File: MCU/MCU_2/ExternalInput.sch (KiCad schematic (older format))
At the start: 49 parts, among them J14 Conn_01x02, J15 Conn_01x02, J16 Conn_01x02, J17 Conn_01x04, J18 Conn_01x02, J20 CAN, J21 Conn_01x04, Q13 DTA144E, Q14 DTA124E, Q15 DTC124E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

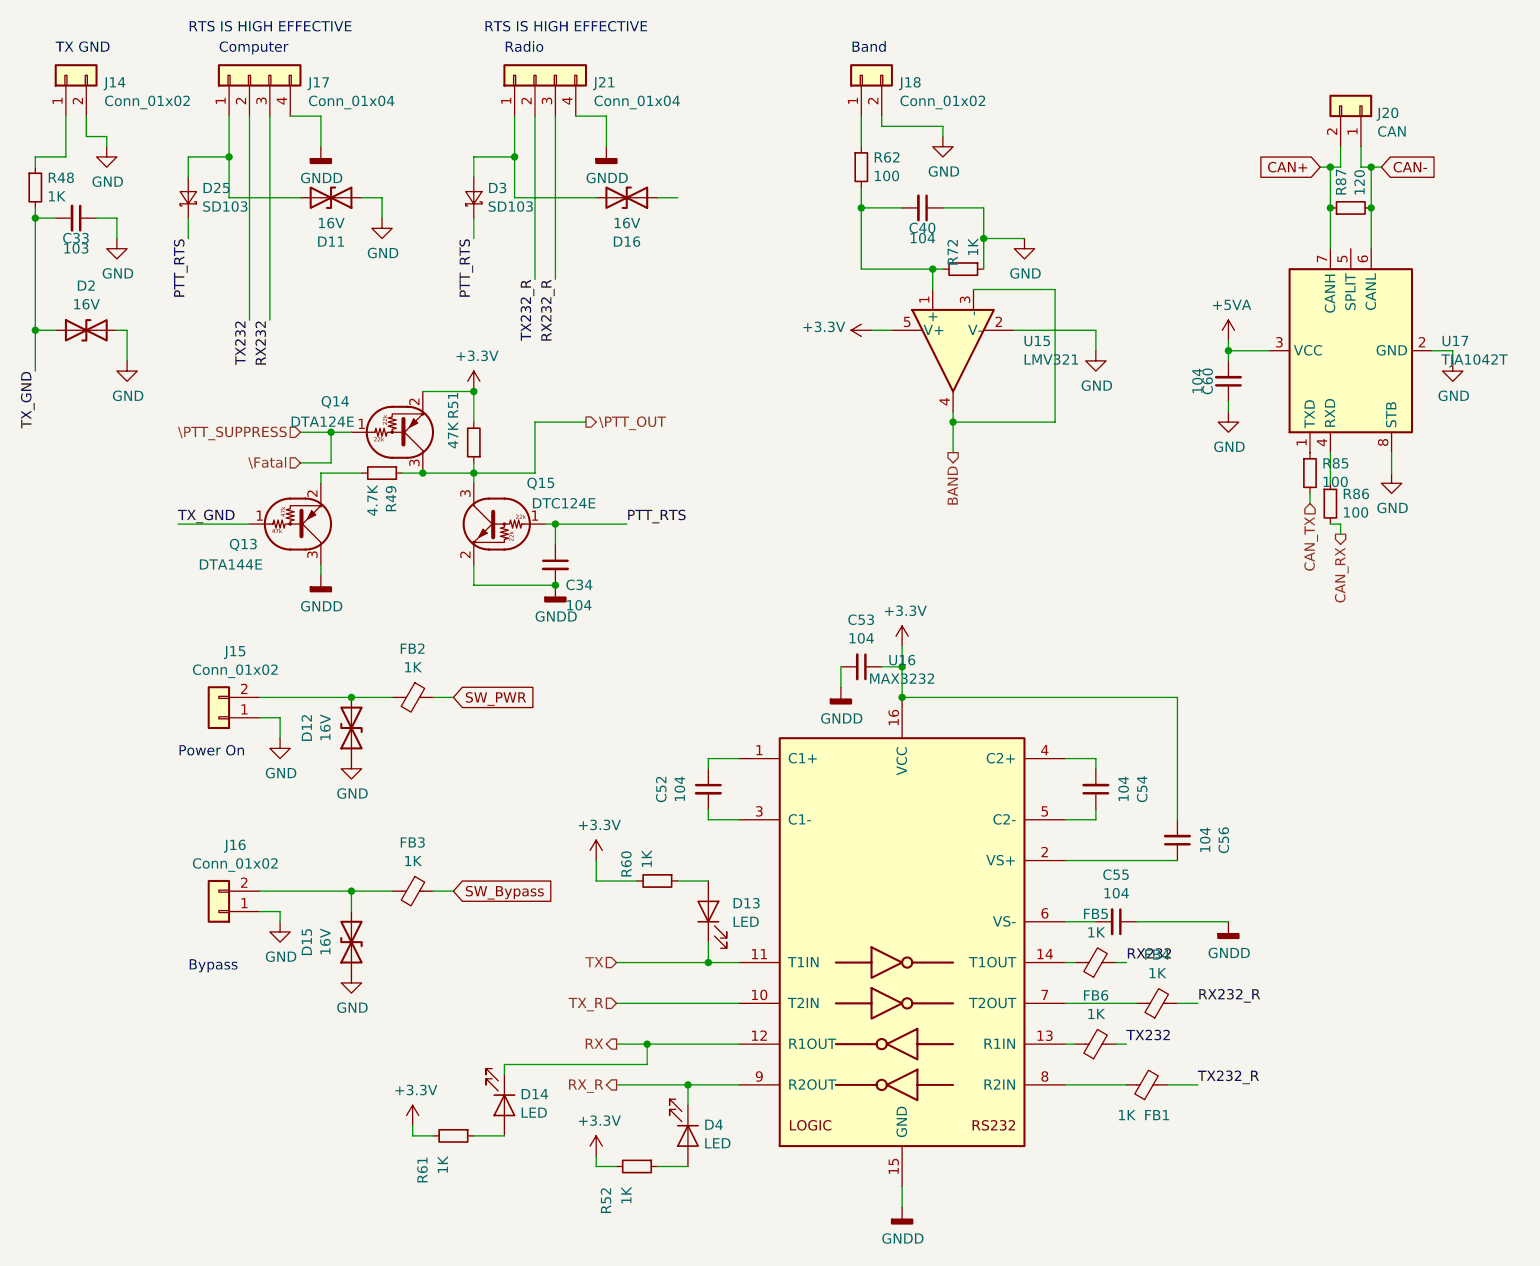
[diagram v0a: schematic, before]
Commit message: MCU PCB start layouting
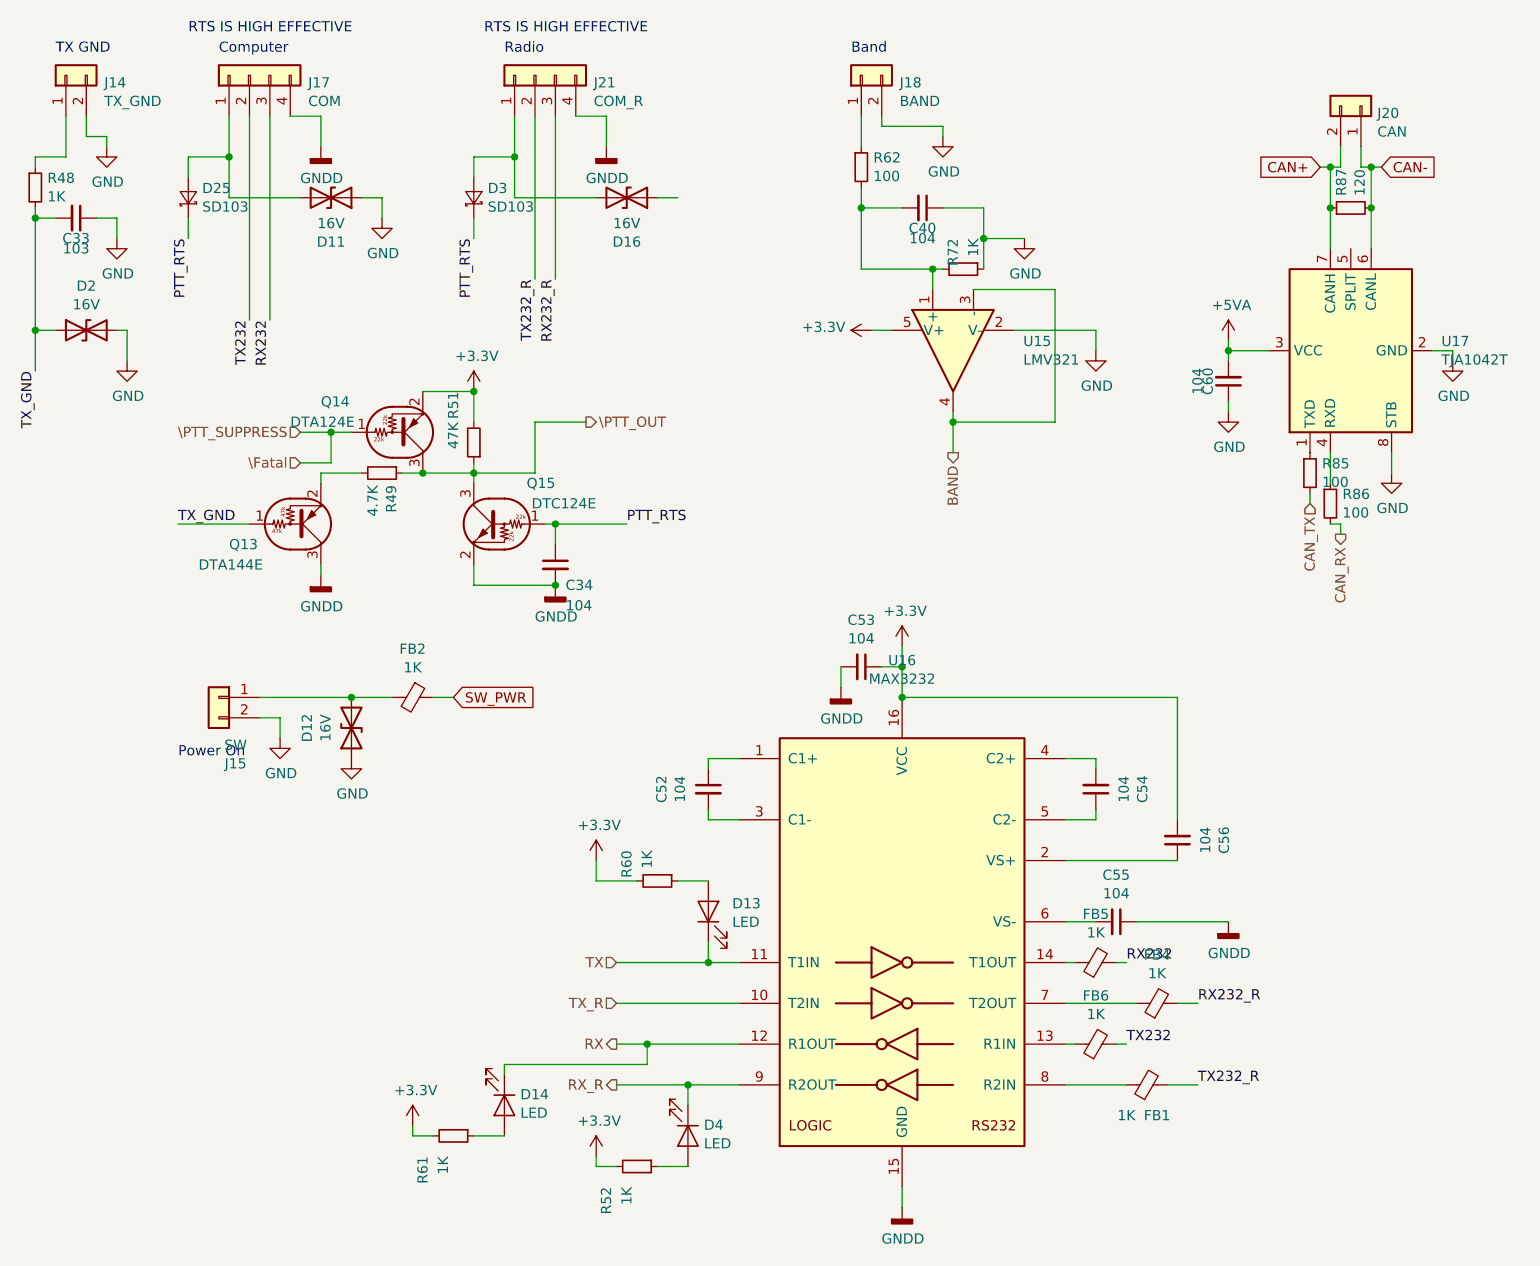
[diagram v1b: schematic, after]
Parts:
- removed D15: 16V, lc_lib:SMA(DO-214AC)_S4, symbol Device:D_TVS
- removed FB3: 1K, lc_lib:0805_R, symbol Device:Ferrite_Bead_Small
- removed J16: Conn_01x02, Connector_PinHeader_2.54mm:PinHeader_1x02_P2.54mm_Vertical, symbol Connector_Generic:Conn_01x02
- J14: value Conn_01x02 -> TX_GND
- J15: value Conn_01x02 -> SW
- J17: value Conn_01x04 -> COM
- J18: value Conn_01x02 -> BAND
- J21: value Conn_01x04 -> COM_R
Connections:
- net GND: now also J15.2 (Pin_2); no longer J15.1 (Pin_1)
- net at D12.2 (A2), FB2.2: now also J15.1 (Pin_1); no longer J15.2 (Pin_2)
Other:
- note removed: "Bypass"
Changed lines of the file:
@@
 AR Path="/5EA95119/5EA99E3C" Ref="J14"  Part="1"
 F 0 "J14" V 914 1812 50  0000 R CNN
-F 1 "Conn_01x02" V 823 1812 50  0000 R CNN
+F 1 "TX_GND" V 823 1812 50  0000 R CNN
 F 2 "Connector_PinHeader_2.54mm:PinHeader_1x02_P2.54mm_Vertical" H 950 2000 50  0001 C CNN
 F 3 "~" H 950 2000 50  0001 C CNN
@@
 AR Path="/5EA95119/5EA99E4D" Ref="J18"  Part="1"
 F 0 "J18" V 4814 1812 50  0000 R CNN
-F 1 "Conn_01x02" V 4723 1812 50  0000 R CNN
+F 1 "BAND" V 4723 1812 50  0000 R CNN
 F 2 "Connector_PinHeader_2.54mm:PinHeader_1x02_P2.54mm_Vertical" H 4850 2000 50  0001 C CNN
 F 3 "~" H 4850 2000 50  0001 C CNN
@@
 L Connector_Generic:Conn_01x02 J?
 U 1 1 5EA9F740
-P 1700 5150
+P 1700 5050
 AR Path="/5E814668/5EA9F740" Ref="J?"  Part="1"
 AR Path="/5EA95119/5EA9F740" Ref="J15"  Part="1"
-F 0 "J15" H 1618 4825 50  0000 C CNN
-F 1 "Conn_01x02" H 1618 4916 50  0000 C CNN
-F 2 "Connector_PinHeader_2.54mm:PinHeader_1x02_P2.54mm_Vertical" H 1700 5150 50  0001 C CNN
-F 3 "~" H 1700 5150 50  0001 C CNN
-	1    1700 5150
-	-1   0    0    1
+F 0 "J15" H 1618 4725 50  0000 C CNN
+F 1 "SW" H 1618 4816 50  0000 C CNN
+F 2 "Connector_PinHeader_2.54mm:PinHeader_1x02_P2.54mm_Vertical" H 1700 5050 50  0001 C CNN
+F 3 "~" H 1700 5050 50  0001 C CNN
+	1    1700 5050
+	-1   0    0    -1
 $EndComp
 $Comp
@@
 Text Notes 1500 5350 0    50   ~ 0
 Power On
-$Comp
-L Connector_Generic:Conn_01x02 J?
-U 1 1 5EAA244F
-P 1700 6100
-AR Path="/5E814668/5EAA244F" Ref="J?"  Part="1"
-AR Path="/5EA95119/5EAA244F" Ref="J16"  Part="1"
-F 0 "J16" H 1618 5775 50  0000 C CNN
-F 1 "Conn_01x02" H 1618 5866 50  0000 C CNN
-F 2 "Connector_PinHeader_2.54mm:PinHeader_1x02_P2.54mm_Vertical" H 1700 6100 50  0001 C CNN
-F 3 "~" H 1700 6100 50  0001 C CNN
-	1    1700 6100
-	-1   0    0    1
-$EndComp
-Text GLabel 2850 6000 2    50   Input ~ 0
-SW_Bypass
-$Comp
-L power:GND #PWR?
-U 1 1 5EAA2C57
-P 2000 6150
-AR Path="/5E814668/5EAA2C57" Ref="#PWR?"  Part="1"
-AR Path="/5EA95119/5EAA2C57" Ref="#PWR097"  Part="1"
-F 0 "#PWR097" H 2000 5900 50  0001 C CNN
-F 1 "GND" H 2005 5977 50  0000 C CNN
-F 2 "" H 2000 6150 50  0001 C CNN
-F 3 "" H 2000 6150 50  0001 C CNN
-	1    2000 6150
-	1    0    0    -1
-$EndComp
-Wire Wire Line
-	2000 6150 2000 6100
-Wire Wire Line
-	2000 6100 1900 6100
-Text Notes 1550 6400 0    50   ~ 0
-Bypass
 Text HLabel 5300 3850 3    50   Output ~ 0
 BAND
@@
 P 1850 2000
 F 0 "J17" V 1814 1712 50  0000 R CNN
-F 1 "Conn_01x04" V 1723 1712 50  0000 R CNN
+F 1 "COM" V 1723 1712 50  0000 R CNN
 F 2 "Connector_JST:JST_PH_B4B-PH-SM4-TB_1x04-1MP_P2.00mm_Vertical" H 1850 2000 50  0001 C CNN
 F 3 "~" H 1850 2000 50  0001 C CNN
@@
 Wire Wire Line
 	800  2400 950  2400
-$Comp
-L Device:Ferrite_Bead_Small FB3
-U 1 1 5E4A8DD2
-P 2650 6000
-F 0 "FB3" V 2413 6000 50  0000 C CNN
-F 1 "1K" V 2504 6000 50  0000 C CNN
-F 2 "lc_lib:0805_R" V 2580 6000 50  0001 C CNN
-F 3 "~" H 2650 6000 50  0001 C CNN
-	1    2650 6000
-	0    1    1    0
-$EndComp
 Wire Wire Line
 	800  2650 800  2700
 Wire Wire Line
 	1550 2700 1550 2800
-Wire Wire Line
-	2750 6000 2850 6000
 $Comp
 L power:GNDD #PWR0146
@@
 P 3250 2000
 F 0 "J21" V 3214 1712 50  0000 R CNN
-F 1 "Conn_01x04" V 3123 1712 50  0000 R CNN
+F 1 "COM_R" V 3123 1712 50  0000 R CNN
 F 2 "Connector_JST:JST_PH_B4B-PH-SM4-TB_1x04-1MP_P2.00mm_Vertical" H 3250 2000 50  0001 C CNN
 F 3 "~" H 3250 2000 50  0001 C CNN
@@
 SW_PWR
 $Comp
-L Device:D_TVS D15
-U 1 1 6188138C
-P 2350 6250
-F 0 "D15" H 2350 6467 50  0000 C CNN
-F 1 "16V" H 2350 6376 50  0000 C CNN
-F 2 "lc_lib:SMA(DO-214AC)_S4" H 2350 6250 50  0001 C CNN
-F 3 "~" H 2350 6250 50  0001 C CNN
-	1    2350 6250
-	0    -1   -1   0
-$EndComp
-$Comp
 L Device:D_TVS D12
 U 1 1 61881392
@@
 	1    0    0    -1
 $EndComp
-Wire Wire Line
-	1900 6000 2350 6000
-Wire Wire Line
-	2350 6100 2350 6000
-Connection ~ 2350 6000
-Wire Wire Line
-	2350 6000 2550 6000
-$Comp
-L power:GND #PWR?
-U 1 1 618B9365
-P 2350 6400
-AR Path="/5E814668/618B9365" Ref="#PWR?"  Part="1"
-AR Path="/5EA95119/618B9365" Ref="#PWR0118"  Part="1"
-F 0 "#PWR0118" H 2350 6150 50  0001 C CNN
-F 1 "GND" H 2355 6227 50  0000 C CNN
-F 2 "" H 2350 6400 50  0001 C CNN
-F 3 "" H 2350 6400 50  0001 C CNN
-	1    2350 6400
-	1    0    0    -1
-$EndComp

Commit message: routing signals
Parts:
- removed C40: 104, lc_lib:0805_C, symbol Device:C_Small
- removed J18: BAND, Connector_PinHeader_2.54mm:PinHeader_1x02_P2.54mm_Vertical, symbol Connector_Generic:Conn_01x02
- removed R62: 100, lc_lib:0805_R, symbol Device:R_Small
- removed R72: 1K, lc_lib:0805_R, symbol Device:R_Small
- removed U15: LMV321, lc_lib:SOT-23-5, symbol Amplifier_Operational:LMV321
- J20: footprint Connector_JST:JST_PH_B2B-PH-SM4-TB_1x02-1MP_P2.00mm_Vertical -> Connector_PinHeader_2.54mm:PinHeader_1x02_P2.54mm_Vertical
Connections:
- net CAN+: now also J20.1 (Pin_1); no longer J20.2 (Pin_2)
- net CAN-: now also J20.2 (Pin_2); no longer J20.1 (Pin_1)
- net GND: now also D16.1 (A1)
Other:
- note removed: "Band"
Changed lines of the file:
@@
 $Descr A4 11693 8268
 encoding utf-8
-Sheet 4 5
+Sheet 3 5
 Title ""
 Date ""
@@
 Wire Wire Line
 	1050 2300 1050 2200
-$Comp
-L Connector_Generic:Conn_01x02 J?
-U 1 1 5EA99E4D
-P 4850 2000
-AR Path="/5E7D94C5/5EA99E4D" Ref="J?"  Part="1"
-AR Path="/5EA95119/5EA99E4D" Ref="J18"  Part="1"
-F 0 "J18" V 4814 1812 50  0000 R CNN
-F 1 "BAND" V 4723 1812 50  0000 R CNN
-F 2 "Connector_PinHeader_2.54mm:PinHeader_1x02_P2.54mm_Vertical" H 4850 2000 50  0001 C CNN
-F 3 "~" H 4850 2000 50  0001 C CNN
-	1    4850 2000
-	0    -1   -1   0
-$EndComp
-$Comp
-L power:GND #PWR?
-U 1 1 5EA99E55
-P 5250 2300
-AR Path="/5E7D94C5/5EA99E55" Ref="#PWR?"  Part="1"
-AR Path="/5EA95119/5EA99E55" Ref="#PWR099"  Part="1"
-F 0 "#PWR099" H 5250 2050 50  0001 C CNN
-F 1 "GND" H 5255 2127 50  0000 C CNN
-F 2 "" H 5250 2300 50  0001 C CNN
-F 3 "" H 5250 2300 50  0001 C CNN
-	1    5250 2300
-	1    0    0    -1
-$EndComp
-Wire Wire Line
-	4950 2250 4950 2200
 $Comp
 L Connector_Generic:Conn_01x02 J?
@@
 Text Notes 1500 5350 0    50   ~ 0
 Power On
-Text HLabel 5300 3850 3    50   Output ~ 0
-BAND
 Wire Wire Line
 	950  2200 950  2400
@@
 $EndComp
 $Comp
-L Device:R_Small R62
-U 1 1 5E2E974A
-P 4850 2450
-F 0 "R62" H 4909 2496 50  0000 L CNN
-F 1 "100" H 4909 2405 50  0000 L CNN
-F 2 "lc_lib:0805_R" H 4850 2450 50  0001 C CNN
-F 3 "~" H 4850 2450 50  0001 C CNN
-	1    4850 2450
-	1    0    0    -1
-$EndComp
-Wire Wire Line
-	4850 2550 4850 2650
-$Comp
-L Device:C_Small C40
-U 1 1 5E2EA49A
-P 5150 2650
-F 0 "C40" V 5250 2650 50  0000 C CNN
-F 1 "104" V 5300 2650 50  0000 C CNN
-F 2 "lc_lib:0805_C" H 5150 2650 50  0001 C CNN
-F 3 "~" H 5150 2650 50  0001 C CNN
-	1    5150 2650
-	0    1    1    0
-$EndComp
-Wire Wire Line
-	5050 2650 4850 2650
-$Comp
-L power:GND #PWR?
-U 1 1 5E2EAA47
-P 5650 2800
-AR Path="/5E7D94C5/5E2EAA47" Ref="#PWR?"  Part="1"
-AR Path="/5EA95119/5E2EAA47" Ref="#PWR0100"  Part="1"
-F 0 "#PWR0100" H 5650 2550 50  0001 C CNN
-F 1 "GND" H 5655 2627 50  0000 C CNN
-F 2 "" H 5650 2800 50  0001 C CNN
-F 3 "" H 5650 2800 50  0001 C CNN
-	1    5650 2800
-	1    0    0    -1
-$EndComp
-Text Notes 4800 1900 0    50   ~ 0
-Band
-$Comp
 L Interface_UART:MAX3232 U16
 U 1 1 5E403A54
@@
 Text HLabel 3650 6750 0    50   Output ~ 0
 RX
-$Comp
-L Device:R_Small R61
-U 1 1 5F387D6B
-P 2850 7200
-F 0 "R61" H 2950 7050 50  0000 L CNN
-F 1 "1K" H 2950 7150 50  0000 L CNN
-F 2 "lc_lib:0805_R" H 2850 7200 50  0001 C CNN
-F 3 "~" H 2850 7200 50  0001 C CNN
-	1    2850 7200
-	0    1    1    0
-$EndComp
 Wire Wire Line
 	3650 6350 4100 6350
@@
 	1    0    0    -1
 $EndComp
-$Comp
-L MySchLib:LED D14
-U 1 1 5E42F239
-P 3100 7050
-F 0 "D14" V 3047 7128 50  0000 L CNN
-F 1 "LED" V 3138 7128 50  0000 L CNN
-F 2 "lc_lib:0805_LED_S1" H 3100 7050 50  0001 C CNN
-F 3 "~" H 3100 7050 50  0001 C CNN
-	1    3100 7050
-	0    1    1    0
-$EndComp
-Wire Wire Line
-	2950 7200 3100 7200
-$Comp
-L power:+3.3V #PWR0127
-U 1 1 5E431F98
-P 2650 7150
-F 0 "#PWR0127" H 2650 7000 50  0001 C CNN
-F 1 "+3.3V" H 2665 7323 50  0000 C CNN
-F 2 "" H 2650 7150 50  0001 C CNN
-F 3 "" H 2650 7150 50  0001 C CNN
-	1    2650 7150
-	1    0    0    -1
-$EndComp
-Wire Wire Line
-	2650 7150 2650 7200
-Wire Wire Line
-	2650 7200 2750 7200
 $Comp
 L power:GNDD #PWR0128
@@
 Wire Wire Line
 	6100 6750 6150 6750
-Wire Wire Line
-	4850 2350 4850 2200
-Wire Wire Line
-	5400 3050 5800 3050
-Wire Wire Line
-	5800 3050 5800 3700
-Wire Wire Line
-	5800 3700 5300 3700
-Wire Wire Line
-	5300 3700 5300 3650
-$Comp
-L power:GND #PWR?
-U 1 1 5E46C360
-P 6000 3350
-AR Path="/5E7D94C5/5E46C360" Ref="#PWR?"  Part="1"
-AR Path="/5EA95119/5E46C360" Ref="#PWR0129"  Part="1"
-F 0 "#PWR0129" H 6000 3100 50  0001 C CNN
-F 1 "GND" H 6005 3177 50  0000 C CNN
-F 2 "" H 6000 3350 50  0001 C CNN
-F 3 "" H 6000 3350 50  0001 C CNN
-	1    6000 3350
-	1    0    0    -1
-$EndComp
-Wire Wire Line
-	6000 3250 6000 3350
-Wire Wire Line
-	5600 3250 6000 3250
-$Comp
-L power:+3.3V #PWR0130
-U 1 1 5E46DBA6
-P 4900 3250
-F 0 "#PWR0130" H 4900 3100 50  0001 C CNN
-F 1 "+3.3V" V 4915 3378 50  0000 L CNN
-F 2 "" H 4900 3250 50  0001 C CNN
-F 3 "" H 4900 3250 50  0001 C CNN
-	1    4900 3250
-	0    -1   -1   0
-$EndComp
-Wire Wire Line
-	4900 3250 5000 3250
-Connection ~ 4850 2650
-$Comp
-L Device:R_Small R72
-U 1 1 5E47FF06
-P 5350 2950
-F 0 "R72" H 5200 2900 50  0000 L CNN
-F 1 "1K" H 5200 3000 50  0000 L CNN
-F 2 "lc_lib:0805_R" H 5350 2950 50  0001 C CNN
-F 3 "~" H 5350 2950 50  0001 C CNN
-	1    5350 2950
-	0    1    1    0
-$EndComp
-Wire Wire Line
-	5200 3050 5200 2950
-Connection ~ 5200 2950
-Wire Wire Line
-	5200 2950 5250 2950
-Wire Wire Line
-	5450 2950 5450 2800
-Wire Wire Line
-	5450 2800 5650 2800
-Wire Wire Line
-	5450 2650 5450 2800
-Wire Wire Line
-	5250 2650 5450 2650
-Connection ~ 5450 2800
-Wire Wire Line
-	4850 2950 5200 2950
-Wire Wire Line
-	5250 2250 5250 2300
-Wire Wire Line
-	4950 2250 5250 2250
-Wire Wire Line
-	5300 3700 5300 3850
-Connection ~ 5300 3700
-$Comp
-L Amplifier_Operational:LMV321 U15
-U 1 1 5E4950BC
-P 5300 3350
-F 0 "U15" V 5254 3006 50  0000 R CNN
-F 1 "LMV321" V 5345 3006 50  0000 R CNN
-F 2 "lc_lib:SOT-23-5" H 5300 3350 50  0001 L CNN
-F 3 "http://www.ti.com/lit/ds/symlink/lmv324.pdf" H 5300 3350 50  0001 C CNN
-	1    5300 3350
-	0    -1   1    0
-$EndComp
 Wire Wire Line
 	1550 2500 1550 2400
@@
 L Connector_Generic:Conn_01x02 J20
 U 1 1 5E54ECE3
-P 7300 2150
-F 0 "J20" V 7264 2230 50  0000 L CNN
-F 1 "CAN" V 7173 2230 50  0000 L CNN
-F 2 "Connector_JST:JST_PH_B2B-PH-SM4-TB_1x02-1MP_P2.00mm_Vertical" H 7300 2150 50  0001 C CNN
-F 3 "~" H 7300 2150 50  0001 C CNN
-	1    7300 2150
-	0    1    -1   0
+P 7200 2150
+F 0 "J20" V 7164 2230 50  0000 L CNN
+F 1 "CAN" V 7073 2230 50  0000 L CNN
+F 2 "Connector_PinHeader_2.54mm:PinHeader_1x02_P2.54mm_Vertical" H 7200 2150 50  0001 C CNN
+F 3 "~" H 7200 2150 50  0001 C CNN
+	1    7200 2150
+	0    -1   -1   0
 $EndComp
 $Comp
@@
 Wire Wire Line
 	3650 6950 4000 6950
-Wire Wire Line
-	3100 6900 3100 6850
-Wire Wire Line
-	3100 6850 3800 6850
 Wire Wire Line
 	3800 6850 3800 6750
@@
 Wire Wire Line
 	2250 3750 2100 3750
-Wire Wire Line
-	4850 2650 4850 2950
 $Comp
 L Device:D_TVS D11
@@
 	-1   0    0    1
 $EndComp
-Wire Wire Line
-	3950 2600 3850 2600
 Wire Wire Line
 	3550 2600 3150 2600
@@
 Wire Wire Line
 	2500 2700 2500 2600
+Wire Wire Line
+	3100 6850 3800 6850
+Wire Wire Line
+	3100 6900 3100 6850
+Wire Wire Line
+	2650 7200 2750 7200
+Wire Wire Line
+	2650 7150 2650 7200
+$Comp
+L power:+3.3V #PWR0127
+U 1 1 5E431F98
+P 2650 7150
+F 0 "#PWR0127" H 2650 7000 50  0001 C CNN
+F 1 "+3.3V" H 2665 7323 50  0000 C CNN
+F 2 "" H 2650 7150 50  0001 C CNN
+F 3 "" H 2650 7150 50  0001 C CNN
+	1    2650 7150
+	1    0    0    -1
+$EndComp
+Wire Wire Line
+	2950 7200 3100 7200
+$Comp
+L MySchLib:LED D14
+U 1 1 5E42F239
+P 3100 7050
+F 0 "D14" V 3047 7128 50  0000 L CNN
+F 1 "LED" V 3138 7128 50  0000 L CNN
+F 2 "lc_lib:0805_LED_S1" H 3100 7050 50  0001 C CNN
+F 3 "~" H 3100 7050 50  0001 C CNN
+	1    3100 7050
+	0    1    1    0
+$EndComp
+$Comp
+L Device:R_Small R61
+U 1 1 5F387D6B
+P 2850 7200
+F 0 "R61" H 2950 7050 50  0000 L CNN
+F 1 "1K" H 2950 7150 50  0000 L CNN
+F 2 "lc_lib:0805_R" H 2850 7200 50  0001 C CNN
+F 3 "~" H 2850 7200 50  0001 C CNN
+	1    2850 7200
+	0    1    1    0
+$EndComp
+$Comp
+L power:GND #PWR?
+U 1 1 6230A516
+P 4000 2700
+AR Path="/5E7D94C5/6230A516" Ref="#PWR?"  Part="1"
+AR Path="/5EA95119/6230A516" Ref="#PWR?"  Part="1"
+F 0 "#PWR?" H 4000 2450 50  0001 C CNN
+F 1 "GND" H 4005 2527 50  0000 C CNN
+F 2 "" H 4000 2700 50  0001 C CNN
+F 3 "" H 4000 2700 50  0001 C CNN
+	1    4000 2700
+	1    0    0    -1
+$EndComp
+Wire Wire Line
+	4000 2700 4000 2600
+Wire Wire Line
+	3850 2600 4000 2600
 $EndSCHEMATC
